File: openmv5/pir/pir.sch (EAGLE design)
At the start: 55 parts, among them IC1 AP3032KTR-G1, IC2 AP3032KTR-G1, J2 OPENMV5-TOP, Q4 2N7002KW_R1_00001, U1 EKMB1307113K, U2 MIC5365-3.3YMT-TZ

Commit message: Renumber parts
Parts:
- removed C46: 4.7uF, sfe:CAP0402-CAP
- removed C48: 0.22uF, rcl:C-EUC0201
- removed C49: 22uF, SparkFun-Capacitors:22UF-0805-6.3V-20%
- removed D9: CPDQT5V0HE-HF, CPDQT5V0HE-HF:CPDQT5V0HE-HF
- added C10, C9: 4.7uF, sfe:CAP0402-CAP
- added C8: 1uF, sfe:CAP0402-CAP
- added D7: CPDQT5V0HE-HF, CPDQT5V0HE-HF:CPDQT5V0HE-HF
- C1: value 4.7uF -> 22uF; device sfe:CAP0402-CAP -> SparkFun-Capacitors:22UF-0805-6.3V-20%; MPN JMK105BBJ475MV-F -> CL21A226MQQNNNE
- C3, C7: value 1uF -> 0.22uF; device sfe:CAP0402-CAP -> rcl:C-EUC0201; MPN GRM155R61H105KE05D -> GRM033R60J224ME15D
- C4: value 22uF -> 1uF; device SparkFun-Capacitors:22UF-0805-6.3V-20% -> sfe:CAP0402-CAP; MPN CL21A226MQQNNNE -> GRM155R61H105KE05D
- C5: value 0.22uF -> 22uF; device rcl:C-EUC0201 -> SparkFun-Capacitors:22UF-0805-6.3V-20%; MPN GRM033R60J224ME15D -> CL21A226MQQNNNE
- D1: value CPDQT5V0HE-HF -> RB520S30T5G; device CPDQT5V0HE-HF:CPDQT5V0HE-HF -> RB520S30T5G:RB520S30T5G; MPN CPDQT5V0HE-HF -> RB520S30T5G
- D5: value RB520S30T5G -> CPDQT5V0HE-HF; device RB520S30T5G:RB520S30T5G -> CPDQT5V0HE-HF:CPDQT5V0HE-HF; MPN RB520S30T5G -> CPDQT5V0HE-HF
- LED11, LED12, LED13, LED9: value SFH_4053 -> JB2835AWT-W-U57EA0000-N0000001; device SFH_4053:SFH_4053 -> JB2835AWT-W-U57EA0000-N0000001:JB2835AWT-W-U57EA0000-N0000001; MPN SFH 4053 -> JB2835AWT-W-U57EA0000-N0000001
- LED3, LED4, LED6, LED8: value JB2835AWT-W-U57EA0000-N0000001 -> SFH_4053; device JB2835AWT-W-U57EA0000-N0000001:JB2835AWT-W-U57EA0000-N0000001 -> SFH_4053:SFH_4053; MPN JB2835AWT-W-U57EA0000-N0000001 -> SFH 4053
- renumbered J2 to J1, Q4 to Q1, R24 to R6, R26 to R5
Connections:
- net GND: now also C10.1, C3.2, C5.1, C7.2, C8.1, C9.1, D5.2, D7.2; no longer C3.1, C46.1, C48.2, C49.1, C5.2, C7.1, D1.2, D9.2
- net I1: now also LED3.A, LED6.K; no longer LED10.A, LED9.K
- net I2: now also LED3.K, LED4.A; no longer LED10.K, LED11.A
- net I3: now also LED4.K, LED8.A; no longer LED11.K, LED12.A
- net I4: now also LED10.A, LED8.K; no longer LED12.K, LED13.A
- net I5: now also LED10.K, LED16.A; no longer LED13.K, LED14.A
- net I6: now also LED16.K; no longer LED14.K
- net I7: now also LED14.A; no longer LED16.A
- net IFB: now also LED14.K; no longer LED16.K
- net IOV: now also C8.2, D2.K, LED6.A; no longer C7.2, D5.K, LED9.A
- net ISW: now also D2.A; no longer D5.A
- net P11_WAKEUP: now also D6.1; no longer D9.1
- net P8_PWM: now also D4.1; no longer D6.1
- net RAW: now also C9.2, D7.1; no longer C1.2, D1.1
- net VCC: now also C1.2, C2.2, C3.1, C5.2, C7.1, D5.1; no longer C4.2, C46.2, C48.1, C49.2, C5.1, D4.1
- net VDD: now also C10.2; no longer C2.2
- net W1: now also LED1.A, LED5.K; no longer LED1.K, LED2.A
- net W2: now also LED1.K, LED2.A; no longer LED2.K, LED3.A
- net W3: now also LED2.K, LED7.A; no longer LED3.K, LED4.A
- net W4: now also LED7.K, LED9.A; no longer LED4.K, LED5.A
- net W5: now also LED13.A, LED9.K; no longer LED5.K, LED6.A
- net W6: now also LED12.A, LED13.K; no longer LED6.K, LED7.A
- net W7: now also LED11.A, LED12.K; no longer LED7.K, LED8.A
- net WFB: now also LED11.K; no longer LED8.K
- net WOV: now also C4.2, D1.K, LED5.A; no longer C3.2, D2.K, LED1.A
- net WSW: now also D1.A; no longer D2.A
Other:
- moved on the sheet: C1, C2, C3, C4, C5, C7, D2, D4, D6, LED1, LED10, LED11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

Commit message: Fix wrogn resistor
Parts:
- R5: MPN 0402WGF1001TCE -> CRCW04021K00FKEDC
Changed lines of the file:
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@@
 </part>
 <part name="R5" library="sfe" deviceset="RESISTOR" device="0402-RES" value="1K">
-<attribute name="MPN" value="0402WGF1001TCE"/>
+<attribute name="MPN" value="CRCW04021K00FKEDC"/>
 </part>
 <part name="RAW1" library="supply" deviceset="RAW" device="" value="RAW"/>

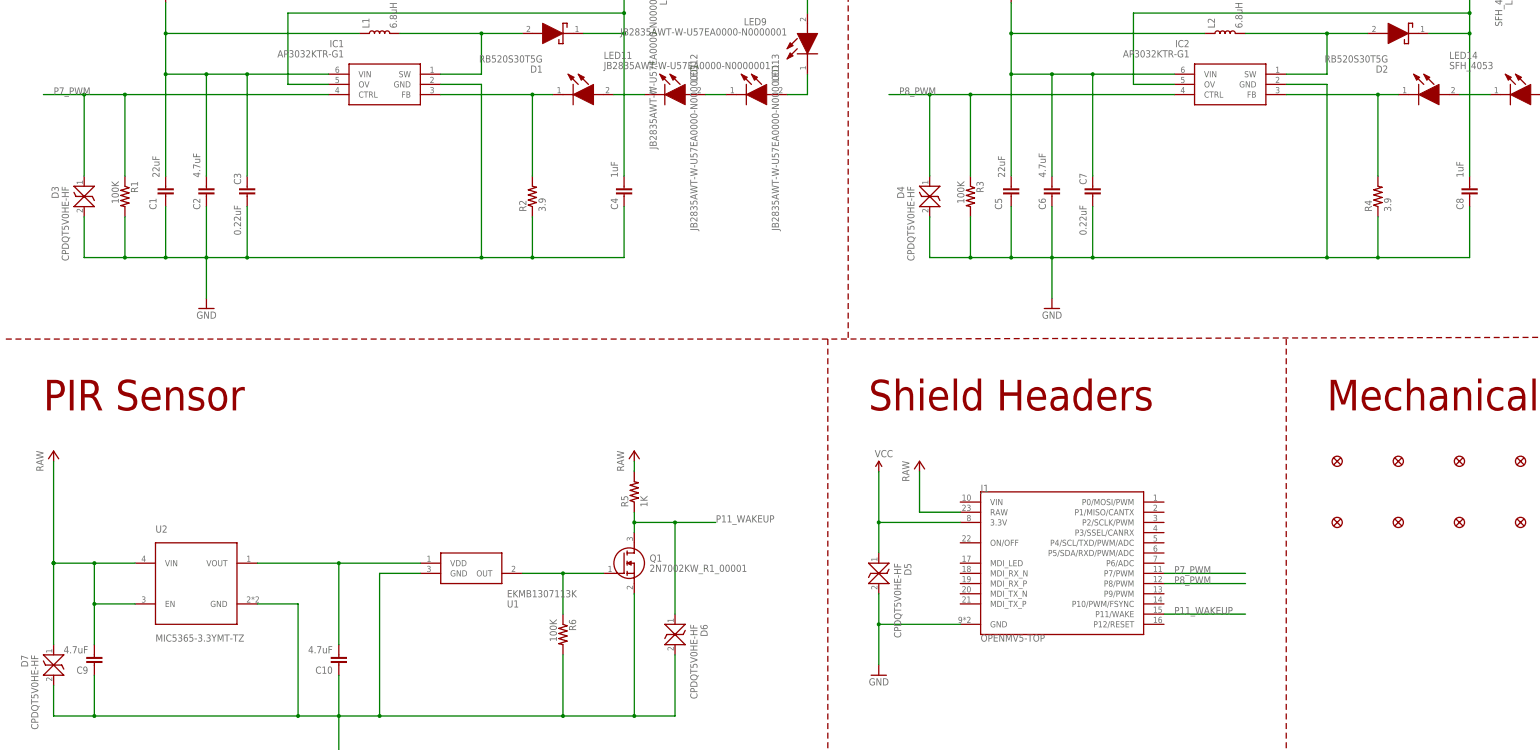
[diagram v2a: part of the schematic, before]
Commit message: Remove 0201 caps
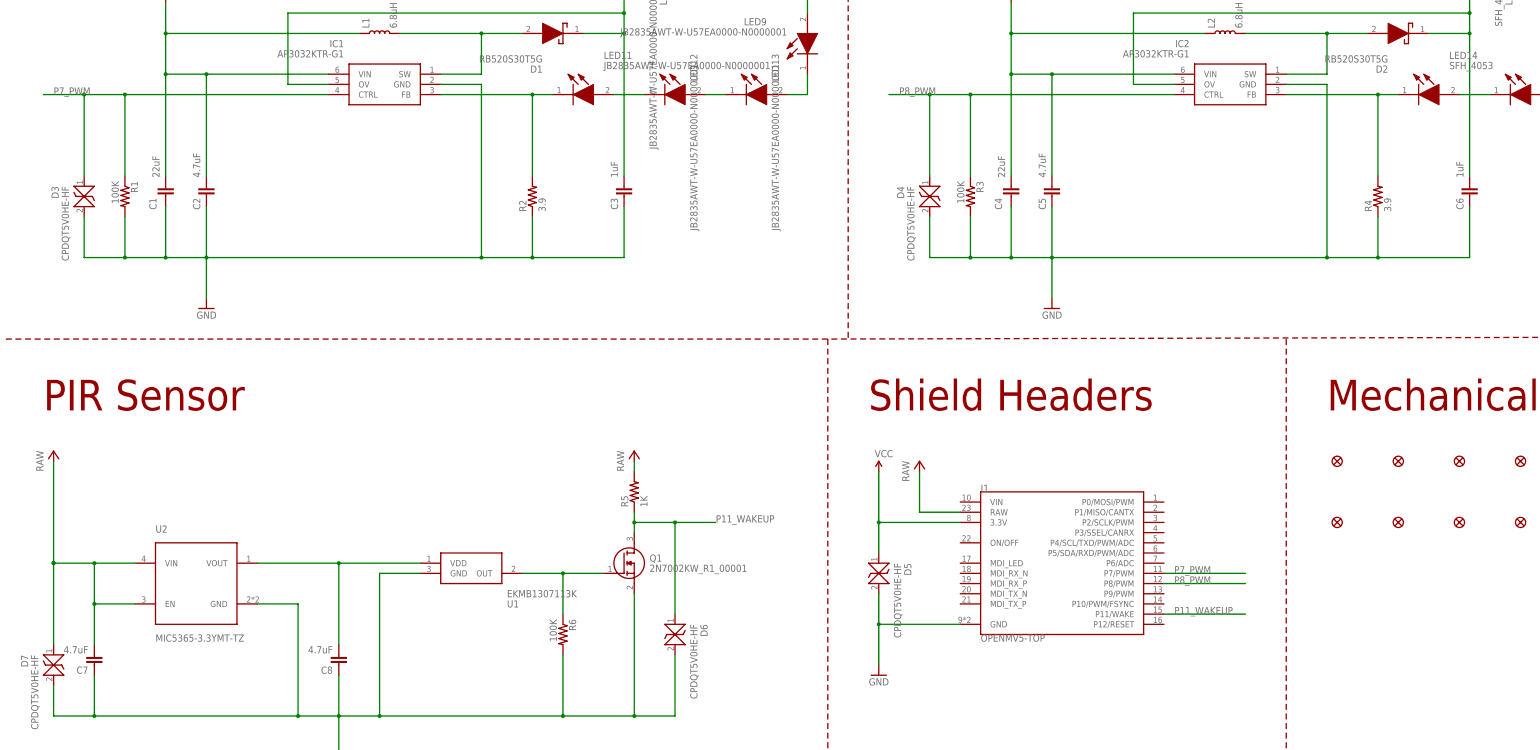
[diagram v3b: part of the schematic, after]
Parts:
- removed C10, C9: 4.7uF, sfe:CAP0402-CAP
- C3: value 0.22uF -> 1uF; device rcl:C-EUC0201 -> sfe:CAP0402-CAP; MPN GRM033R60J224ME15D -> GRM155R61H105KE05D
- C4: value 1uF -> 22uF; device sfe:CAP0402-CAP -> SparkFun-Capacitors:22UF-0805-6.3V-20%; MPN GRM155R61H105KE05D -> CL21A226MQQNNNE
- C5: value 22uF -> 4.7uF; device SparkFun-Capacitors:22UF-0805-6.3V-20% -> sfe:CAP0402-CAP; MPN CL21A226MQQNNNE -> JMK105BBJ475MV-F
- C6: value 4.7uF -> 1uF; MPN JMK105BBJ475MV-F -> GRM155R61H105KE05D
- C7: value 0.22uF -> 4.7uF; device rcl:C-EUC0201 -> sfe:CAP0402-CAP; MPN GRM033R60J224ME15D -> JMK105BBJ475MV-F
- C8: value 1uF -> 4.7uF; MPN GRM155R61H105KE05D -> JMK105BBJ475MV-F
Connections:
- net GND: now also C3.1, C7.1; no longer C10.1, C3.2, C7.2, C9.1
- net IOV: now also C6.2; no longer C8.2
- net RAW: now also C7.2; no longer C9.2
- net VCC: now also C4.2; no longer C3.1, C6.2, C7.1
- net VDD: now also C8.2; no longer C10.2
- net WOV: now also C3.2; no longer C4.2
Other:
- moved on the sheet: C3, C4, C5, C6, C7, C8

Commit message: Add bypasses
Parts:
- added JP1, JP2, JP3: JUMPER-SMT_2_NC_PASTE_SILK, SparkFun-Jumpers:JUMPER-SMT_2_NC_PASTE_SILK
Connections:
- new net P11_WAKEUP_INT: J1.P11/WAKE, JP3.1
- new net P7_PWM_INT: J1.P7/PWM, JP1.1
- new net P8_PWM_INT: J1.P8/PWM, JP2.1
- net P11_WAKEUP: now also JP3.2; no longer J1.P11/WAKE
- net P7_PWM: now also JP1.2; no longer J1.P7/PWM
- net P8_PWM: now also JP2.2; no longer J1.P8/PWM
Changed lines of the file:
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@@
 <attribute name="MPN" value="SFH 4053"/>
 </part>
+<part name="JP1" library="SparkFun-Jumpers" library_urn="urn:adsk.eagle:library:528" deviceset="JUMPER-SMT_2_NC_PASTE" device="_SILK" package3d_urn="urn:adsk.eagle:package:39282/1"/>
+<part name="JP2" library="SparkFun-Jumpers" library_urn="urn:adsk.eagle:library:528" deviceset="JUMPER-SMT_2_NC_PASTE" device="_SILK" package3d_urn="urn:adsk.eagle:package:39282/1"/>
+<part name="JP3" library="SparkFun-Jumpers" library_urn="urn:adsk.eagle:library:528" deviceset="JUMPER-SMT_2_NC_PASTE" device="_SILK" package3d_urn="urn:adsk.eagle:package:39282/1"/>
 </parts>
 <sheets>
@@
 <text x="7.62" y="15.24" size="5.08" layer="97">This work is licensed under the Creative Commons Attribution-ShareAlike 3.0 License.</text>
 <text x="7.62" y="5.08" size="5.08" layer="97">To view a copy of this license, visit http://creativecommons.org/licenses/by-sa/3.0/</text>
-<wire x1="325.12" y1="35.56" x2="5.08" y2="35.56" width="0.1524" layer="94" style="longdash"/>
+<wire x1="345.44" y1="35.56" x2="5.08" y2="35.56" width="0.1524" layer="94" style="longdash"/>
 <text x="15.24" y="256.54" size="7.62" layer="94" font="vector" ratio="20">White LED Driver</text>
 <wire x1="210.82" y1="157.48" x2="5.08" y2="157.48" width="0.1524" layer="94" style="longdash"/>
@@
 <wire x1="210.82" y1="157.48" x2="210.82" y2="35.56" width="0.1524" layer="94" style="longdash"/>
 <wire x1="426.212" y1="157.988" x2="210.82" y2="157.48" width="0.1524" layer="94" style="longdash"/>
-<text x="335.28" y="139.7" size="7.62" layer="94" font="vector" ratio="20">Mechanical</text>
+<text x="355.6" y="139.7" size="7.62" layer="94" font="vector" ratio="20">Mechanical</text>
 <text x="226.06" y="256.54" size="7.62" layer="94" font="vector" ratio="20">IR LED Driver</text>
-<wire x1="325.12" y1="157.48" x2="325.12" y2="35.56" width="0.1524" layer="94" style="longdash"/>
+<wire x1="345.44" y1="157.48" x2="345.44" y2="35.56" width="0.1524" layer="94" style="longdash"/>
 <text x="220.98" y="139.7" size="7.62" layer="94" font="vector" ratio="20">Shield Headers</text>
-<wire x1="223.52" y1="53.34" x2="322.58" y2="53.34" width="0.1524" layer="150" style="longdash"/>
-<wire x1="322.58" y1="53.34" x2="322.58" y2="38.1" width="0.1524" layer="150" style="longdash"/>
-<wire x1="322.58" y1="38.1" x2="223.52" y2="38.1" width="0.1524" layer="150" style="longdash"/>
-<wire x1="223.52" y1="38.1" x2="223.52" y2="53.34" width="0.1524" layer="150" style="longdash"/>
-<text x="226.06" y="40.64" size="2.54" layer="150" font="vector" ratio="20">* The LEDs are powered by the 3.3V rail so
+<wire x1="243.84" y1="53.34" x2="342.9" y2="53.34" width="0.1524" layer="150" style="longdash"/>
+<wire x1="342.9" y1="53.34" x2="342.9" y2="38.1" width="0.1524" layer="150" style="longdash"/>
+<wire x1="342.9" y1="38.1" x2="243.84" y2="38.1" width="0.1524" layer="150" style="longdash"/>
+<wire x1="243.84" y1="38.1" x2="243.84" y2="53.34" width="0.1524" layer="150" style="longdash"/>
+<text x="246.38" y="40.64" size="2.54" layer="150" font="vector" ratio="20">* The LEDs are powered by the 3.3V rail so
 that they do not draw any current when the
 main 3.3V regulator is turned off.</text>
@@
 <attribute name="DRAWING_NAME" x="342.9" y="19.05" size="2.54" layer="94"/>
 </instance>
-<instance part="FD1" gate="G$1" x="337.82" y="127" smashed="yes"/>
-<instance part="FD5" gate="G$1" x="337.82" y="111.76" smashed="yes"/>
-<instance part="FD6" gate="G$1" x="353.06" y="111.76" smashed="yes"/>
-<instance part="FD2" gate="G$1" x="353.06" y="127" smashed="yes"/>
-<instance part="FD3" gate="G$1" x="368.3" y="127" smashed="yes"/>
-<instance part="FD7" gate="G$1" x="368.3" y="111.76" smashed="yes"/>
-<instance part="FD4" gate="G$1" x="383.54" y="127" smashed="yes"/>
-<instance part="FD8" gate="G$1" x="383.54" y="111.76" smashed="yes"/>
+<instance part="FD1" gate="G$1" x="358.14" y="127" smashed="yes"/>
+<instance part="FD5" gate="G$1" x="358.14" y="111.76" smashed="yes"/>
+<instance part="FD6" gate="G$1" x="373.38" y="111.76" smashed="yes"/>
+<instance part="FD2" gate="G$1" x="373.38" y="127" smashed="yes"/>
+<instance part="FD3" gate="G$1" x="388.62" y="127" smashed="yes"/>
+<instance part="FD7" gate="G$1" x="388.62" y="111.76" smashed="yes"/>
+<instance part="FD4" gate="G$1" x="403.86" y="127" smashed="yes"/>
+<instance part="FD8" gate="G$1" x="403.86" y="111.76" smashed="yes"/>
 <instance part="U1" gate="G$1" x="109.22" y="99.06" smashed="yes" rot="MR180">
 <attribute name="NAME" x="130.81" y="91.44" size="1.778" layer="95" rot="MR180" align="center-left"/>
@@
 <attribute name="VALUE" x="365.76" y="224.79" size="1.778" layer="96"/>
 <attribute name="MPN" x="353.06" y="218.44" size="1.778" layer="96" display="off"/>
+</instance>
+<instance part="JP1" gate="G$1" x="304.8" y="99.06" smashed="yes">
+<attribute name="NAME" x="302.26" y="101.6" size="1.778" layer="95" font="vector"/>
+<attribute name="VALUE" x="302.26" y="96.52" size="1.778" layer="96" font="vector" align="top-left"/>
+</instance>
+<instance part="JP2" gate="G$1" x="304.8" y="96.52" smashed="yes">
+<attribute name="NAME" x="302.26" y="99.06" size="1.778" layer="95" font="vector"/>
+<attribute name="VALUE" x="302.26" y="93.98" size="1.778" layer="96" font="vector" align="top-left"/>
+</instance>
+<instance part="JP3" gate="G$1" x="304.8" y="88.9" smashed="yes">
+<attribute name="NAME" x="302.26" y="91.44" size="1.778" layer="95" font="vector"/>
+<attribute name="VALUE" x="302.26" y="86.36" size="1.778" layer="96" font="vector" align="top-left"/>
 </instance>
 </instances>
@@
 </segment>
 <segment>
-<pinref part="J1" gate="G$1" pin="P11/WAKE"/>
-<wire x1="294.64" y1="88.9" x2="314.96" y2="88.9" width="0.1524" layer="91"/>
-<label x="297.18" y="88.9" size="1.778" layer="95"/>
+<wire x1="309.88" y1="88.9" x2="335.28" y2="88.9" width="0.1524" layer="91"/>
+<pinref part="JP3" gate="G$1" pin="2"/>
+<label x="314.96" y="88.9" size="1.778" layer="95"/>
 </segment>
 </net>
@@
 </segment>
 <segment>
-<pinref part="J1" gate="G$1" pin="P7/PWM"/>
-<wire x1="294.64" y1="99.06" x2="314.96" y2="99.06" width="0.1524" layer="91"/>
-<label x="297.18" y="99.06" size="1.778" layer="95"/>
+<wire x1="309.88" y1="99.06" x2="335.28" y2="99.06" width="0.1524" layer="91"/>
+<pinref part="JP1" gate="G$1" pin="2"/>
+<label x="314.96" y="99.06" size="1.778" layer="95"/>
 </segment>
 </net>
@@
 <net name="P8_PWM" class="4">
 <segment>
-<pinref part="J1" gate="G$1" pin="P8/PWM"/>
-<wire x1="294.64" y1="96.52" x2="314.96" y2="96.52" width="0.1524" layer="91"/>
-<label x="297.18" y="96.52" size="1.778" layer="95"/>
+<wire x1="309.88" y1="96.52" x2="335.28" y2="96.52" width="0.1524" layer="91"/>
+<pinref part="JP2" gate="G$1" pin="2"/>
+<label x="314.96" y="96.52" size="1.778" layer="95"/>
 </segment>
 <segment>
@@
 </segment>
 </net>
+<net name="P7_PWM_INT" class="4">
+<segment>
+<pinref part="J1" gate="G$1" pin="P7/PWM"/>
+<wire x1="294.64" y1="99.06" x2="299.72" y2="99.06" width="0.1524" layer="91"/>
+<pinref part="JP1" gate="G$1" pin="1"/>
+</segment>
+</net>
+<net name="P8_PWM_INT" class="4">
+<segment>
+<pinref part="J1" gate="G$1" pin="P8/PWM"/>
+<wire x1="294.64" y1="96.52" x2="299.72" y2="96.52" width="0.1524" layer="91"/>
+<pinref part="JP2" gate="G$1" pin="1"/>
+</segment>
+</net>
+<net name="P11_WAKEUP_INT" class="4">
+<segment>
+<pinref part="J1" gate="G$1" pin="P11/WAKE"/>
+<wire x1="294.64" y1="88.9" x2="299.72" y2="88.9" width="0.1524" layer="91"/>
+<pinref part="JP3" gate="G$1" pin="1"/>
+</segment>
+</net>
